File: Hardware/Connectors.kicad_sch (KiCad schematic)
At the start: 41 parts, among them J10 USB_C_Receptacle, J13 JST_Locking_6, J14 Qwiic_Vertical, J2 SMA_Edge, J3 Conn_01x15, J4 Conn_01x18, J5 JST_Locking_6, J6 SMA_Edge, J7 USB_C_Receptacle, J8 U.FL, J9 U.FL

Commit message: Routing WIP
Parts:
- removed TR1: RFCMF1220100M4T, SparkFun-Coil:RFCMF1220100M4T, symbol SparkFun-Coil:USB_Transformer
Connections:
- net USB2_D+: now also D17.3 (I/O2), D17.4 (I/O3), J7.A6 (D+), J7.B6 (D+), TP9.1
- net USB2_D-: now also D17.1 (I/O1), D17.6 (I/O4), J7.A7 (D-), J7.B7 (D-), TP12.1
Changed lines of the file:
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@@
 	(wire
 		(pts
-			(xy 247.65 115.57) (xy 248.92 115.57)
-		)
-		(stroke
-			(width 0)
-			(type default)
-		)
-	)
-	(wire
-		(pts
 			(xy 142.24 52.07) (xy 142.24 60.96)
 		)
@@
 	(wire
 		(pts
-			(xy 247.65 113.03) (xy 248.92 113.03)
-		)
-		(stroke
-			(width 0)
-			(type default)
-		)
-	)
-	(wire
-		(pts
 			(xy 195.58 33.02) (xy 195.58 34.29)
 		)
@@
 	(global_label "USB2_D-"
 		(shape bidirectional)
-		(at 248.92 115.57 0)
+		(at 237.49 115.57 0)
 		(fields_autoplaced yes)
 		(effects
@@
 		)
 		(property "Intersheetrefs" "${INTERSHEET_REFS}"
-			(at 261.846 115.57 0)
+			(at 250.416 115.57 0)
 			(effects
 				(font
@@
 	(global_label "USB2_D+"
 		(shape bidirectional)
-		(at 248.92 113.03 0)
+		(at 237.49 113.03 0)
 		(fields_autoplaced yes)
 		(effects
@@
 		)
 		(property "Intersheetrefs" "${INTERSHEET_REFS}"
-			(at 261.846 113.03 0)
+			(at 250.416 113.03 0)
 			(effects
 				(font
@@
 					(unit 1)
 				)
-			)
-		)
-	)
-	(symbol
-		(lib_id "SparkFun-Coil:USB_Transformer")
-		(at 242.57 114.3 0)
-		(mirror x)
-		(unit 1)
-		(exclude_from_sim no)
-		(in_bom yes)
-		(on_board yes)
-		(dnp no)
-		(property "Reference" "TR1"
-			(at 242.57 110.49 0)
-			(effects
-				(font
-					(size 1.27 1.27)
-				)
-			)
-		)
-		(property "Value" "RFCMF1220100M4T"
-			(at 243.84 118.11 0)
-			(effects
-				(font
-					(size 1.27 1.27)
-				)
-			)
-		)
-		(property "Footprint" "SparkFun-Coil:RFCMF1220100M4T"
-			(at 241.3 107.95 0)
-			(effects
-				(font
-					(size 1.27 1.27)
-				)
-				(hide yes)
-			)
-		)
-		(property "Datasheet" "http://www.passivecomponent.com/wp-content/uploads/2018/10/RF-Filter.pdf"
-			(at 241.3 105.41 0)
-			(effects
-				(font
-					(size 1.27 1.27)
-				)
-				(hide yes)
-			)
-		)
-		(property "Description" "USB Transformer"
-			(at 242.57 100.33 0)
-			(effects
-				(font
-					(size 1.27 1.27)
-				)
-				(hide yes)
-			)
-		)
-		(property "PROD_ID" "COMP-19495"
-			(at 241.3 102.87 0)
-			(effects
-				(font
-					(size 1.27 1.27)
-				)
-				(hide yes)
-			)
-		)
-		(pin "1"
-		)
-		(pin "2"
-		)
-		(pin "4"
-		)
-		(pin "3"
-		)
-		(instances
-			(project ""
-				(path "/e3dd3ae4-244d-4cba-9cca-5d2abf83f29a/31a2c60b-91be-4113-ae16-f797035e304d"
-					(reference "TR1")
-					(unit 1)
-				)

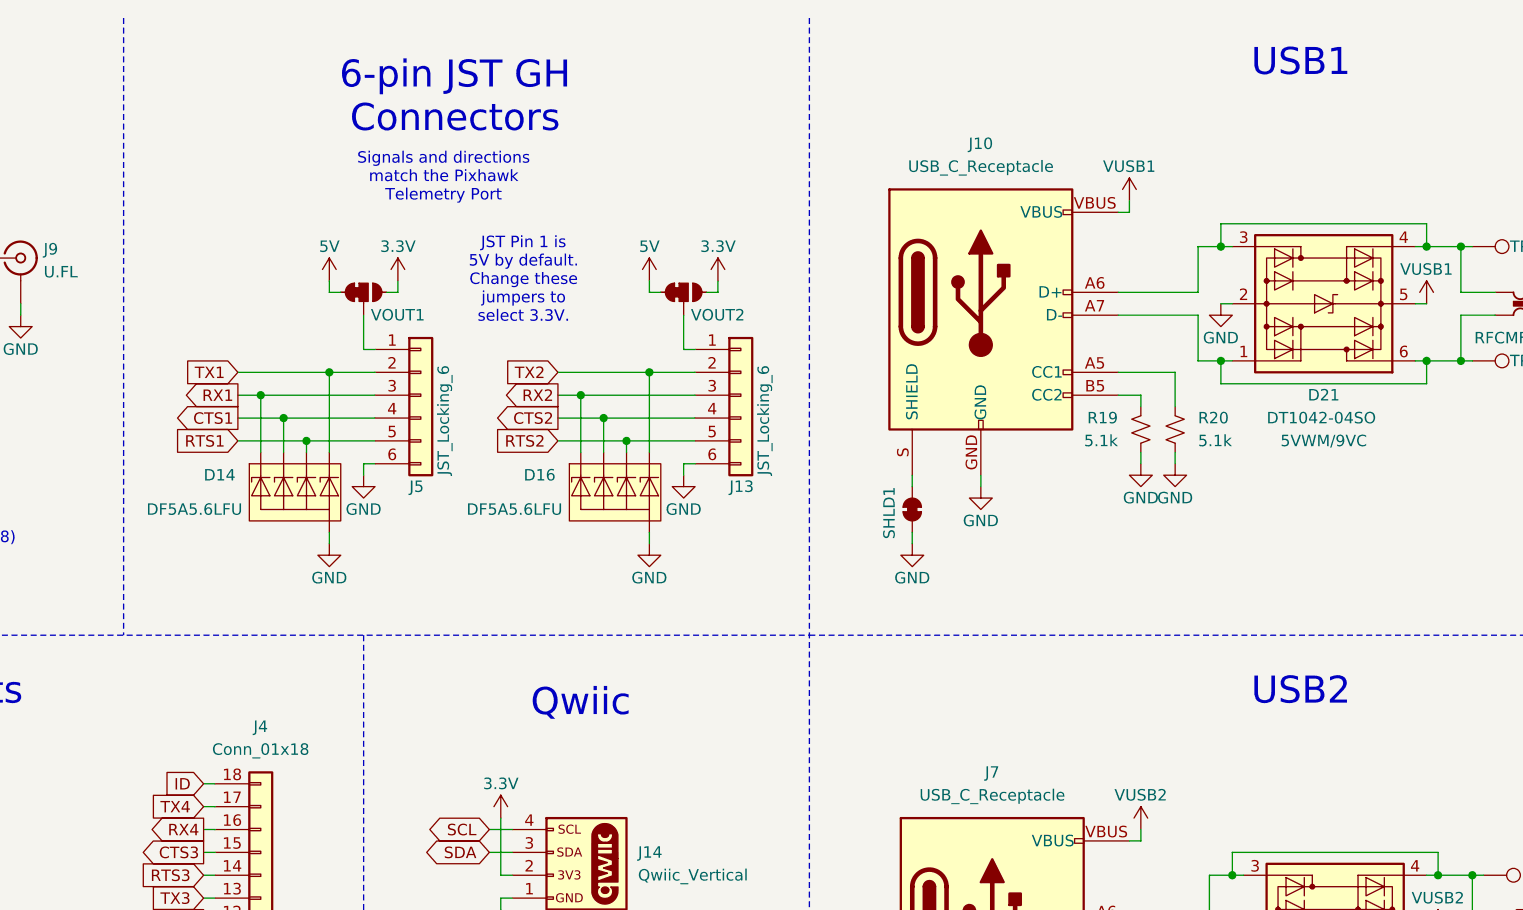
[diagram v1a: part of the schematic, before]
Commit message: Routed and panelized
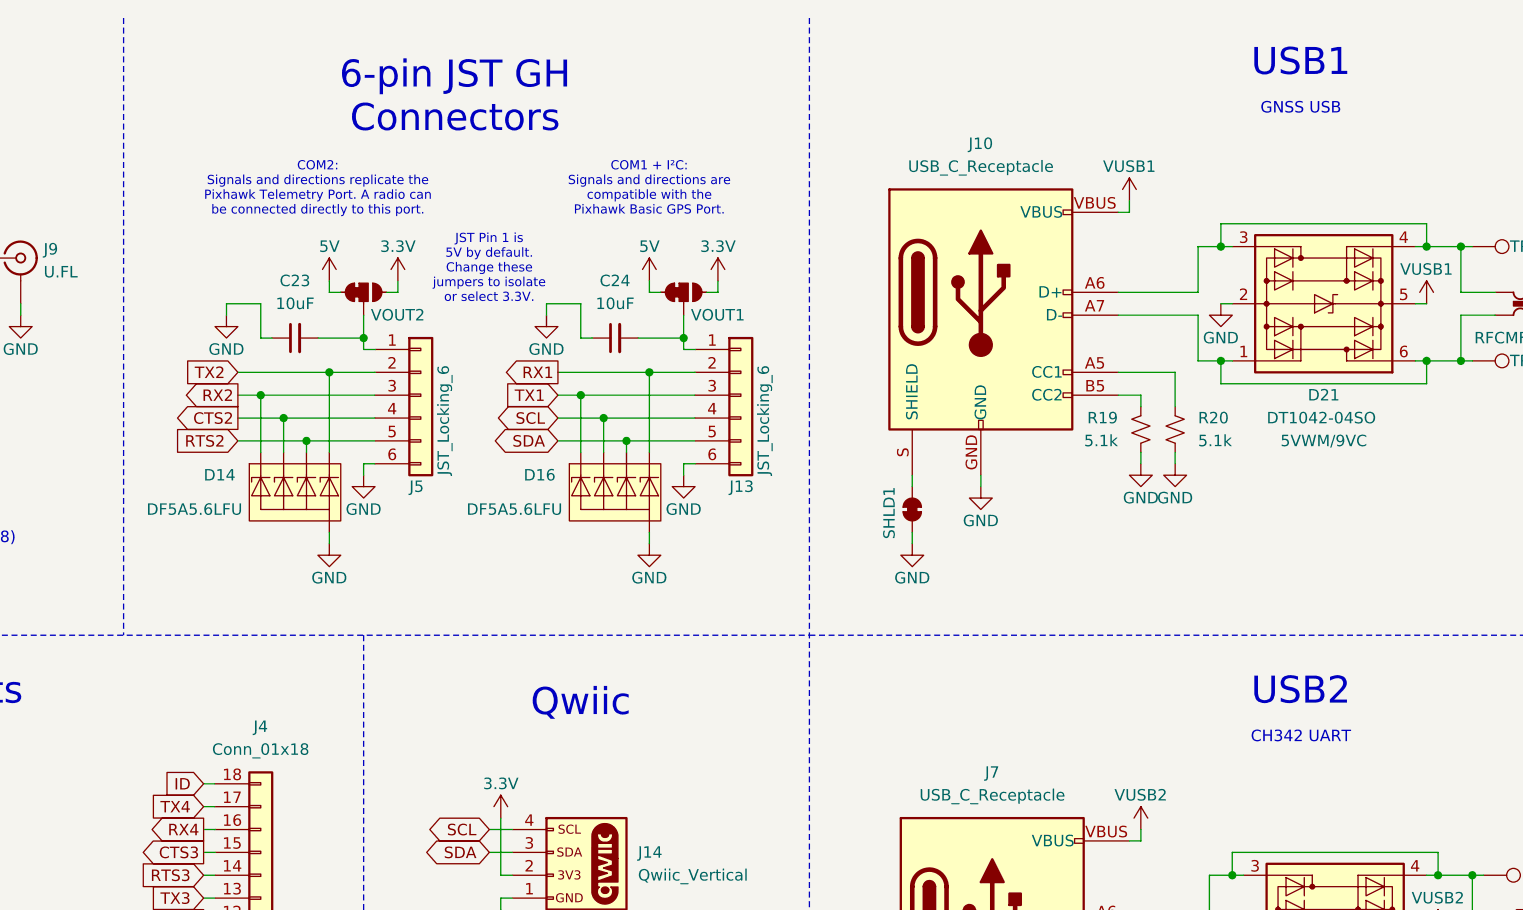
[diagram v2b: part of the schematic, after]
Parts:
- added C23, C24: 10uF, SparkFun-Capacitor:C_0603_1608Metric, symbol SparkFun-Capacitor:10uF_0603_10V_20%
- renumbered VOUT2 to VOUT1, VOUT1 to VOUT2
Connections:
- net CTS1: no longer D14.3 (K2), J5.4 (Pin_4)
- net CTS2: now also D14.3 (K2), J5.4 (Pin_4); no longer D16.3 (K2), J13.4 (Pin_4)
- net GND: now also C23.1, C24.1
- net RTS1: no longer D14.4 (K3), J5.5 (Pin_5)
- net RTS2: now also D14.4 (K3), J5.5 (Pin_5); no longer D16.4 (K3), J13.5 (Pin_5)
- net RX1: now also D16.5 (K4), J13.2 (Pin_2); no longer D14.1 (K1), J5.3 (Pin_3)
- net RX2: now also D14.1 (K1), J5.3 (Pin_3); no longer D16.1 (K1), J13.3 (Pin_3)
- net SCL: now also D16.3 (K2), J13.4 (Pin_4)
- net SDA: now also D16.4 (K3), J13.5 (Pin_5)
- net TX1: now also D16.1 (K1), J13.3 (Pin_3); no longer D14.5 (K4), J5.2 (Pin_2)
- net TX2: now also D14.5 (K4), J5.2 (Pin_2); no longer D16.5 (K4), J13.2 (Pin_2)
- net at J5.1 (Pin_1), VOUT2.2 (B): now also C23.2
- net at J13.1 (Pin_1), VOUT1.2 (B): now also C24.2
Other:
- note added: "CH342 UART"
- note added: "COM1 + I²C: Signals and directions are compatible with the Pixhawk Basic GPS Port."
- note added: "COM2: Signals and directions replicate the Pixhawk Telemetry Port. A radio can be connected directly to this port."
- note added: "GNSS USB"
- note added: "JST Pin 1 is 5V by default. Change these jumpers to isolate or select 3.3V."
- note removed: "JST Pin 1 is 5V by default. Change these jumpers to select 3.3V."
- note removed: "Signals and directions match the Pixhawk Telemetry Port"

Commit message: Updates after proto review
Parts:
- J4: footprint SparkFun-Connector:1x18 -> SparkFun-Connector:1x19; symbol SparkFun-Connector:Conn_01x18 -> SparkFun-Connector:Conn_01x19
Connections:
- net GND: now also J4.19 (Pin_19)
- net VBATT renamed VBACKUP
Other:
- note added: "Note: the antenna GNDs are isolated from each other and the other board GNDs. Antenna GND is connected through the u.FL cables only - to avoid ground loops."
- moved on the sheet: C23, C24, D14, D16, D20, D9, J13, J2, J5, J6, J8, J9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

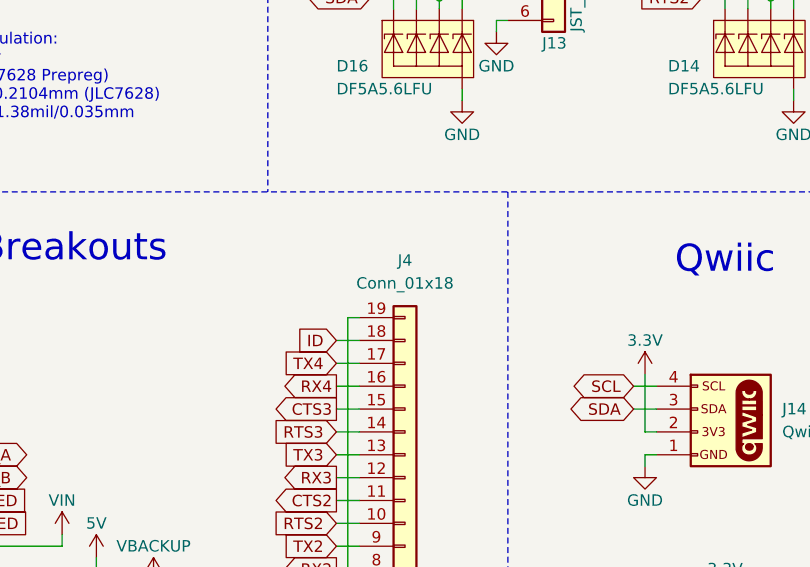
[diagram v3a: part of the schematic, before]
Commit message: PCB v02 - with corrected regulator footprint
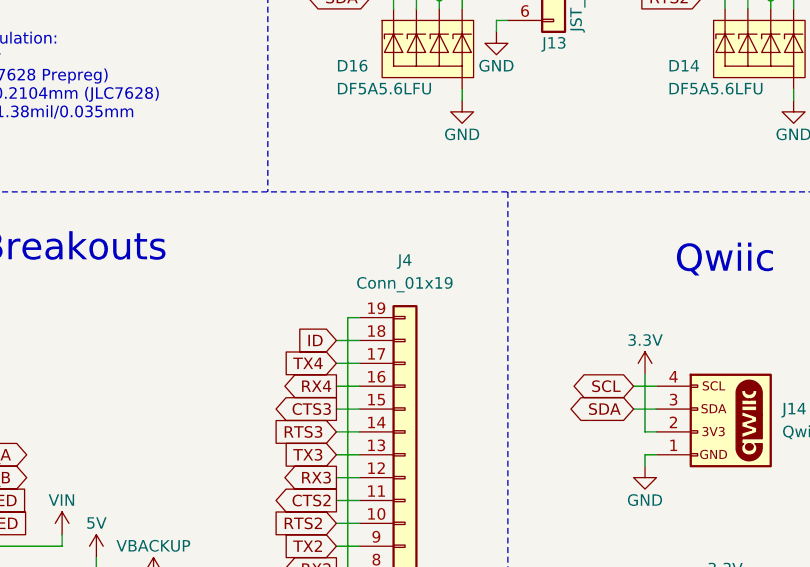
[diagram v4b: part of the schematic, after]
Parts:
- J4: value Conn_01x18 -> Conn_01x19
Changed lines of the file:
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@@
 			)
 		)
-		(property "Value" "Conn_01x18"
+		(property "Value" "Conn_01x19"
 			(at 99.06 91.44 0)
 			(effects
